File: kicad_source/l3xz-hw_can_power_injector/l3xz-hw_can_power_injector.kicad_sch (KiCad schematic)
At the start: 36 parts, among them CN1 Conn_01x02, CN2 Conn_01x04, CN3 Conn_01x04, CN4 Conn_01x02, CN5 Conn_01x04, CN6 Conn_01x04, U1 RAA211650

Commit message: changed connector for input, added connector for VCC
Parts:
- added CN7: Conn_01x02, Connector_PinHeader_2.54mm:PinHeader_1x02_P2.54mm_Vertical, symbol Connector_Generic:Conn_01x02
- CN1: footprint Connector_Wago:Wago_734-132_1x02_P3.50mm_Vertical -> Connector_Phoenix_MC:PhoenixContact_MC_1,5_2-G-3.5_1x02_P3.50mm_Horizontal
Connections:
- net GND: now also CN7.2 (Pin_2)
- net VCC: now also CN7.1 (Pin_1)
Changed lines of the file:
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@@
+    (stroke (width 0) (type default) (color 0 0 0 0))
+  )
+  (wire (pts (xy 154.94 54.61) (xy 154.94 57.15))
     (stroke (width 0) (type default) (color 0 0 0 0))
   )
@@
     (stroke (width 0) (type default) (color 0 0 0 0))
   )
+  (wire (pts (xy 152.4 52.07) (xy 154.94 52.07))
+    (stroke (width 0) (type default) (color 0 0 0 0))
+  )
   (wire (pts (xy 29.21 30.48) (xy 29.21 33.02))
     (stroke (width 0) (type default) (color 0 0 0 0))
@@
     (stroke (width 0) (type default) (color 0 0 0 0))
   )
+  (wire (pts (xy 152.4 54.61) (xy 154.94 54.61))
+    (stroke (width 0) (type default) (color 0 0 0 0))
+  )
   (wire (pts (xy 190.5 101.6) (xy 186.69 101.6))
     (stroke (width 0) (type default) (color 0 0 0 0))
   )
   (wire (pts (xy 95.25 82.55) (xy 97.79 82.55))
+    (stroke (width 0) (type default) (color 0 0 0 0))
+  )
+  (wire (pts (xy 154.94 52.07) (xy 154.94 49.53))
     (stroke (width 0) (type default) (color 0 0 0 0))
   )
@@
     )
     (property "Datasheet" "" (id 3) (at 71.12 24.13 0)
+      (effects (font (size 1.27 1.27)) hide)
+    )
+    (pin "1")
+  )
+  (symbol (lib_id "power:GND") (at 154.94 57.15 0) (unit 1)
+    (in_bom yes) (on_board yes) (fields_autoplaced)
+    (property "Reference" "#PWR042" (id 0) (at 154.94 63.5 0)
+      (effects (font (size 1.27 1.27)) hide)
+    )
+    (property "Value" "GND" (id 1) (at 154.94 62.23 0))
+    (property "Footprint" "" (id 2) (at 154.94 57.15 0)
+      (effects (font (size 1.27 1.27)) hide)
+    )
+    (property "Datasheet" "" (id 3) (at 154.94 57.15 0)
       (effects (font (size 1.27 1.27)) hide)
     )
@@
     (pin "2")
   )
+  (symbol (lib_id "power:VCC") (at 154.94 49.53 0) (unit 1)
+    (in_bom yes) (on_board yes) (fields_autoplaced)
+    (property "Reference" "#PWR041" (id 0) (at 154.94 53.34 0)
+      (effects (font (size 1.27 1.27)) hide)
+    )
+    (property "Value" "VCC" (id 1) (at 154.94 44.45 0))
+    (property "Footprint" "" (id 2) (at 154.94 49.53 0)
+      (effects (font (size 1.27 1.27)) hide)
+    )
+    (property "Datasheet" "" (id 3) (at 154.94 49.53 0)
+      (effects (font (size 1.27 1.27)) hide)
+    )
+    (pin "1")
+  )
   (symbol (lib_id "Mechanical:MountingHole_Pad") (at 69.85 189.23 0) (unit 1)
     (in_bom yes) (on_board yes) (fields_autoplaced)
@@
     (pin "1")
   )
+  (symbol (lib_id "Connector_Generic:Conn_01x02") (at 147.32 52.07 0) (mirror y) (unit 1)
+    (in_bom yes) (on_board yes) (fields_autoplaced)
+    (property "Reference" "CN7" (id 0) (at 147.32 45.72 0))
+    (property "Value" "Conn_01x02" (id 1) (at 147.32 48.26 0))
+    (property "Footprint" "Connector_PinHeader_2.54mm:PinHeader_1x02_P2.54mm_Vertical" (id 2) (at 147.32 52.07 0)
+      (effects (font (size 1.27 1.27)) hide)
+    )
+    (property "Datasheet" "~" (id 3) (at 147.32 52.07 0)
+      (effects (font (size 1.27 1.27)) hide)
+    )
+    (pin "1")
+    (pin "2")
+  )
   (symbol (lib_id "power:VCC") (at 121.92 110.49 0) (unit 1)
     (in_bom yes) (on_board yes) (fields_autoplaced)
@@
     (property "Reference" "CN1" (id 0) (at 39.37 21.59 0))
     (property "Value" "Conn_01x02" (id 1) (at 39.37 24.13 0))
-    (property "Footprint" "Connector_Wago:Wago_734-132_1x02_P3.50mm_Vertical" (id 2) (at 39.37 27.94 0)
+    (property "Footprint" "Connector_Phoenix_MC:PhoenixContact_MC_1,5_2-G-3.5_1x02_P3.50mm_Horizontal" (id 2) (at 39.37 27.94 0)
       (effects (font (size 1.27 1.27)) hide)
     )
@@
       (reference "#PWR040") (unit 1) (value "GND") (footprint "")
     )
+    (path "/a59e06f9-75ca-46d1-b1ec-24a1ea01855c"
+      (reference "#PWR041") (unit 1) (value "VCC") (footprint "")
+    )
+    (path "/528c7a91-ee0f-41c1-bd9d-d68f5b2158cb"
+      (reference "#PWR042") (unit 1) (value "GND") (footprint "")
+    )
     (path "/5fed680c-7375-4ebc-bb86-a241d3c8e39a"
       (reference "C1") (unit 1) (value "C_Small") (footprint "Capacitor_SMD:C_1210_3225Metric")
@@
     )
     (path "/fef5535b-a542-4028-a074-282a4f9c934c"
-      (reference "CN1") (unit 1) (value "Conn_01x02") (footprint "Connector_Wago:Wago_734-132_1x02_P3.50mm_Vertical")
+      (reference "CN1") (unit 1) (value "Conn_01x02") (footprint "Connector_Phoenix_MC:PhoenixContact_MC_1,5_2-G-3.5_1x02_P3.50mm_Horizontal")
     )
     (path "/1d8efb76-5792-410a-946b-8844fea07a7b"
@@
       (reference "CN6") (unit 1) (value "Conn_01x04") (footprint "Connector_JST:JST_GH_BM04B-GHS-TBT_1x04-1MP_P1.25mm_Vertical")
     )
+    (path "/c24b320e-8d6f-4818-8abf-2ea614d47673"
+      (reference "CN7") (unit 1) (value "Conn_01x02") (footprint "Connector_PinHeader_2.54mm:PinHeader_1x02_P2.54mm_Vertical")
+    )
     (path "/30254fe3-40de-4291-a9a6-9c309259cf5f"

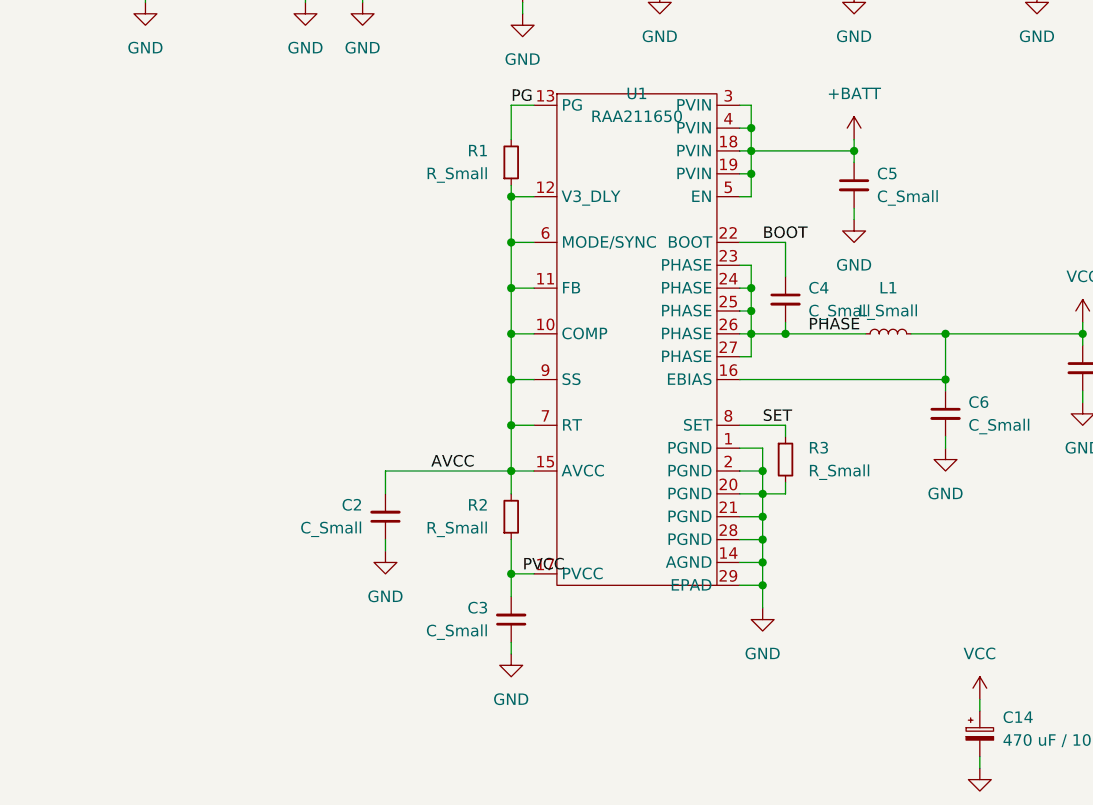
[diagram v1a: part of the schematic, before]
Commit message: updated and set analog values of switching regulator
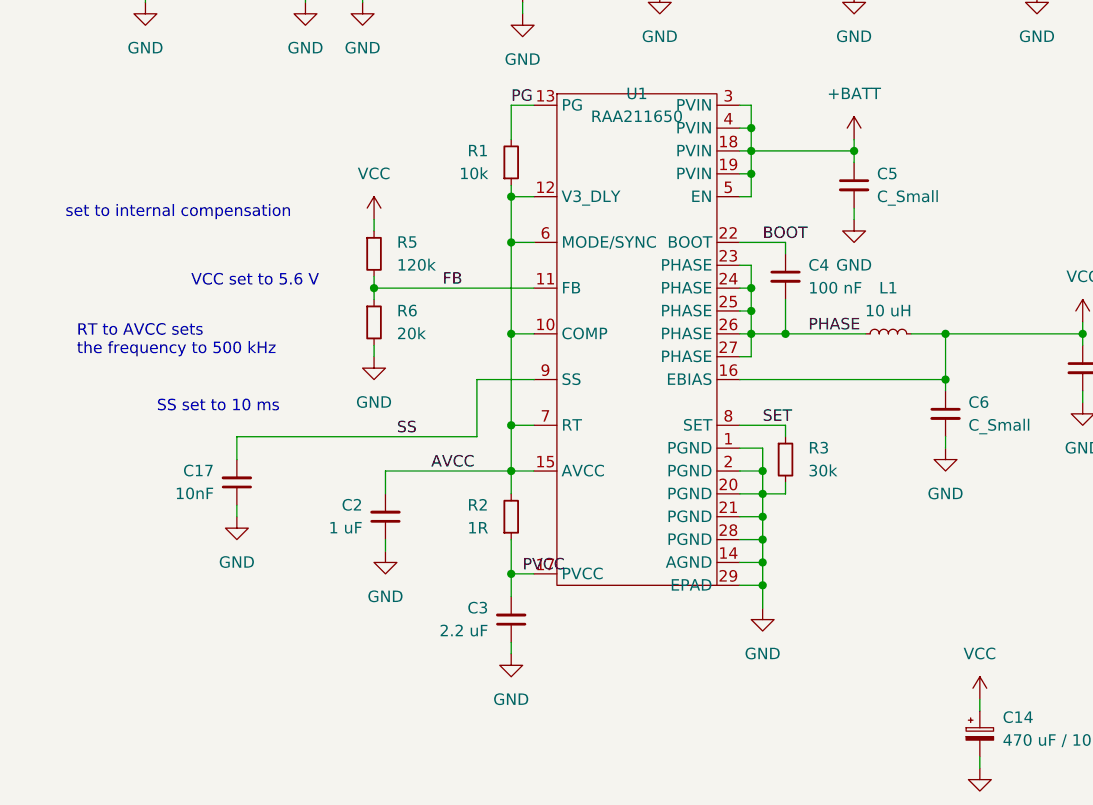
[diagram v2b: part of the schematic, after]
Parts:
- added C17: 10nF, Capacitor_SMD:C_0603_1608Metric, symbol Device:C_Small
- added R5: 120k, Resistor_SMD:R_0603_1608Metric, symbol Device:R_Small
- added R6: 20k, Resistor_SMD:R_0603_1608Metric, symbol Device:R_Small
- C2: value C_Small -> 1 uF
- C3: value C_Small -> 2.2 uF
- C4: value C_Small -> 100 nF
- L1: value L_Small -> 10 uH
- R1: value R_Small -> 10k
- R2: value R_Small -> 1R
- R3: value R_Small -> 30k
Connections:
- net AVCC: no longer U1.11 (FB), U1.9 (SS)
- net GND: now also C17.1, R6.2
- net VCC: now also R5.1
- new net FB: R5.2, R6.1, U1.11 (FB)
- new net SS: C17.2, U1.9 (SS)
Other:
- note added: "RT to AVCC sets the frequency to 500 kHz"
- note added: "SS set to 10 ms"
- note added: "VCC set to 5.6 V"
- note added: "set to internal compensation"
- moved on the sheet: C4

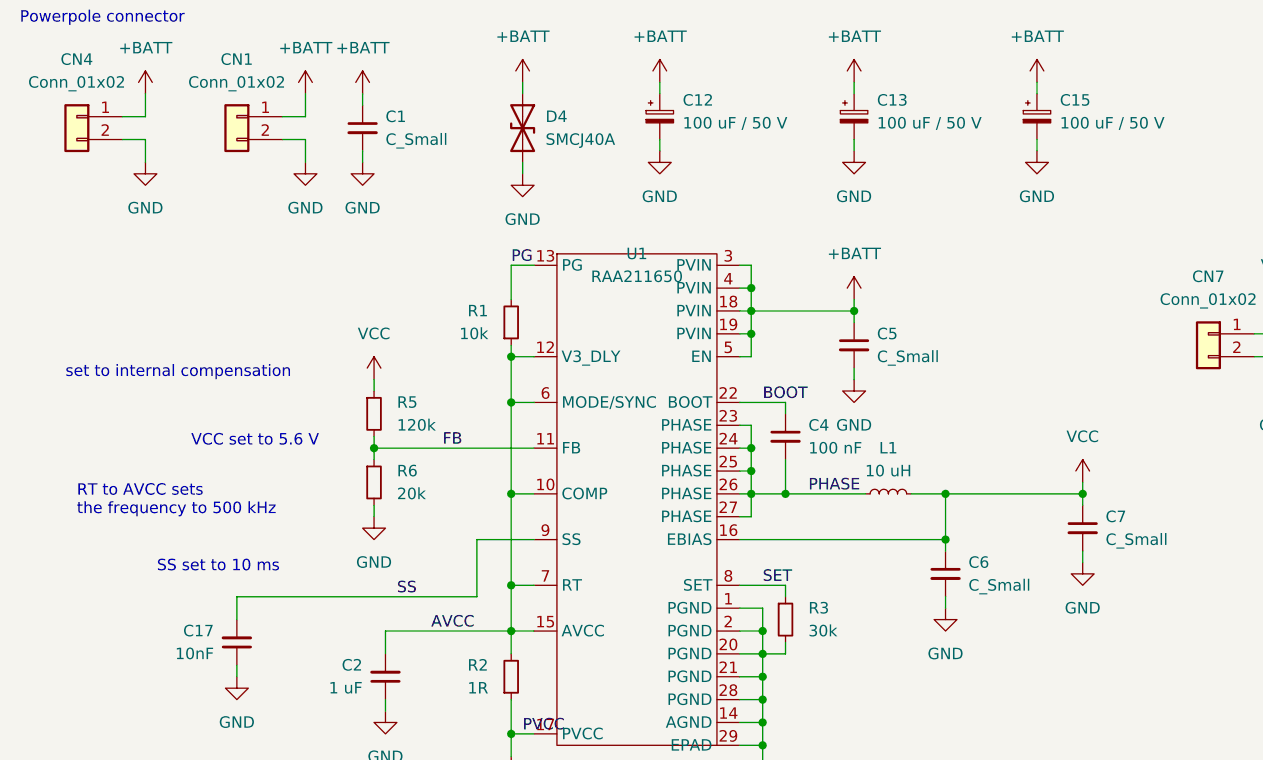
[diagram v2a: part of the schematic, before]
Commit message: added enable on VIN
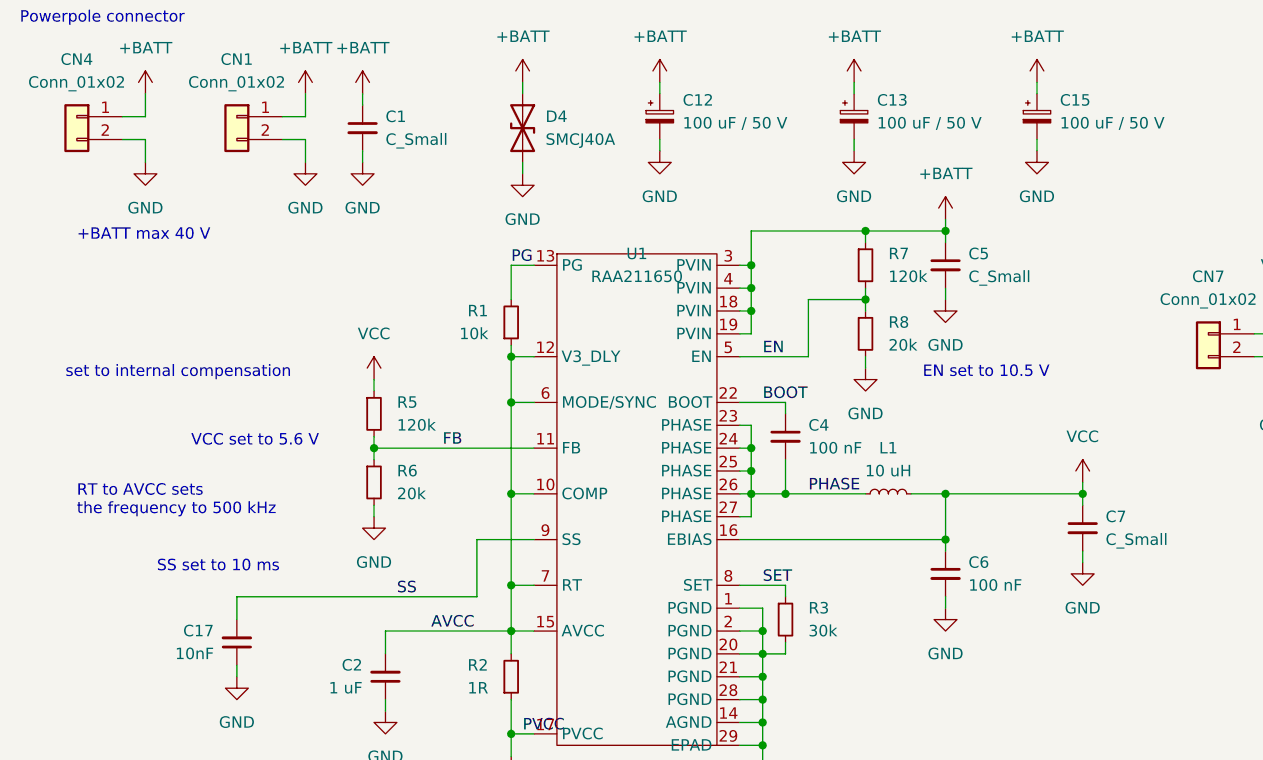
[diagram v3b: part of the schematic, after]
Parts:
- added R7: 120k, Resistor_SMD:R_0603_1608Metric, symbol Device:R_Small
- added R8: 20k, Resistor_SMD:R_0603_1608Metric, symbol Device:R_Small
- C6: value C_Small -> 100 nF
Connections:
- net +BATT: now also R7.1; no longer U1.5 (EN)
- net GND: now also R8.2
- new net EN: R7.2, R8.1, U1.5 (EN)
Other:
- note added: "+BATT max 40 V"
- note added: "EN set to 10.5 V"
- moved on the sheet: C5
